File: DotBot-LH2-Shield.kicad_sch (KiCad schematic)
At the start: 23 parts, among them J1 Conn_01x04, J1 Conn_01x10, U1 74LVC3G34, U3 ISM330DHCXTR, U4 LIS3MDL, U4 TS4231

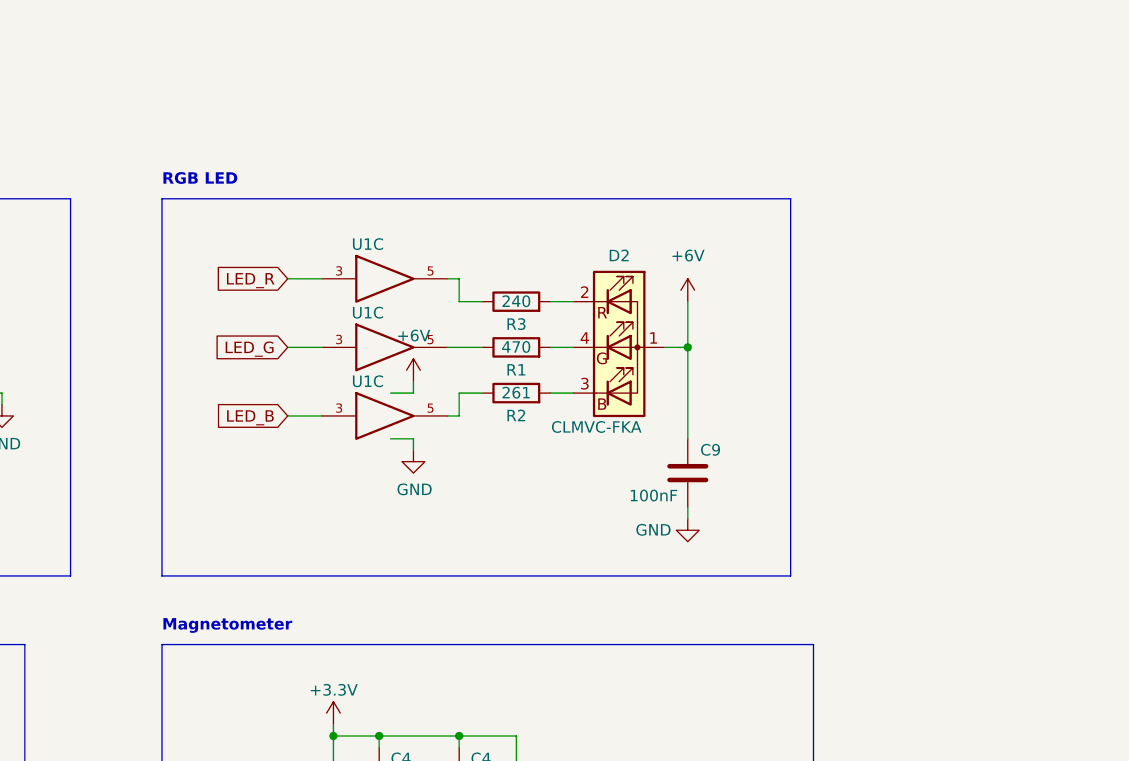
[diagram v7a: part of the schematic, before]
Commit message: fix: reworked led driver circuit schematic
It should now work with 6v supply, and the 1.8v I/O from the nRF
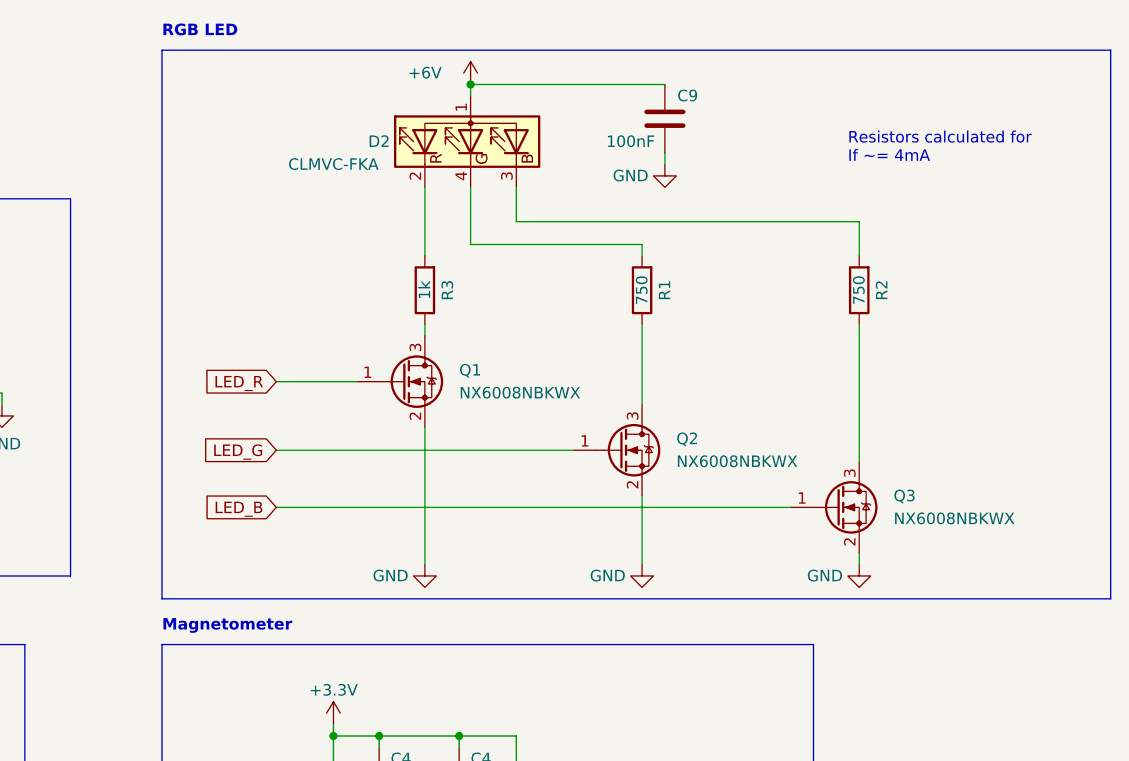
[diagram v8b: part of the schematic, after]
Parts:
- removed U1 (x3): 74LVC3G34, DotBot:SOT833-1-8_1x1.95_Pitch0.5mm, symbol 74xGxx:74LVC3G34
- added Q1, Q2, Q3: NX6008NBKWX, Package_TO_SOT_SMD:SOT-323_SC-70, symbol Device:Q_NMOS_GSD
- R1: value 470 -> 750
- R2: value 261 -> 750
- R3: value 240 -> 1k
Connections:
- net GND: now also Q1.2 (S), Q2.2 (S), Q3.2 (S)
- net LED_B: now also Q3.1 (G)
- net LED_G: now also Q2.1 (G)
- net LED_R: now also Q1.1 (G)
- net at R1.1: now also Q2.3 (D)
- net at R2.1: now also Q3.3 (D)
- net at R3.1: now also Q1.3 (D)
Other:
- note added: "Resistors calculated for If ~= 4mA"
- moved on the sheet: C9, D2, R1, R2, R3
